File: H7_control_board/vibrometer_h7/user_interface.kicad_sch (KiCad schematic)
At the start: 10 parts, among them SW501 SW_Push, SW502 SW_Push

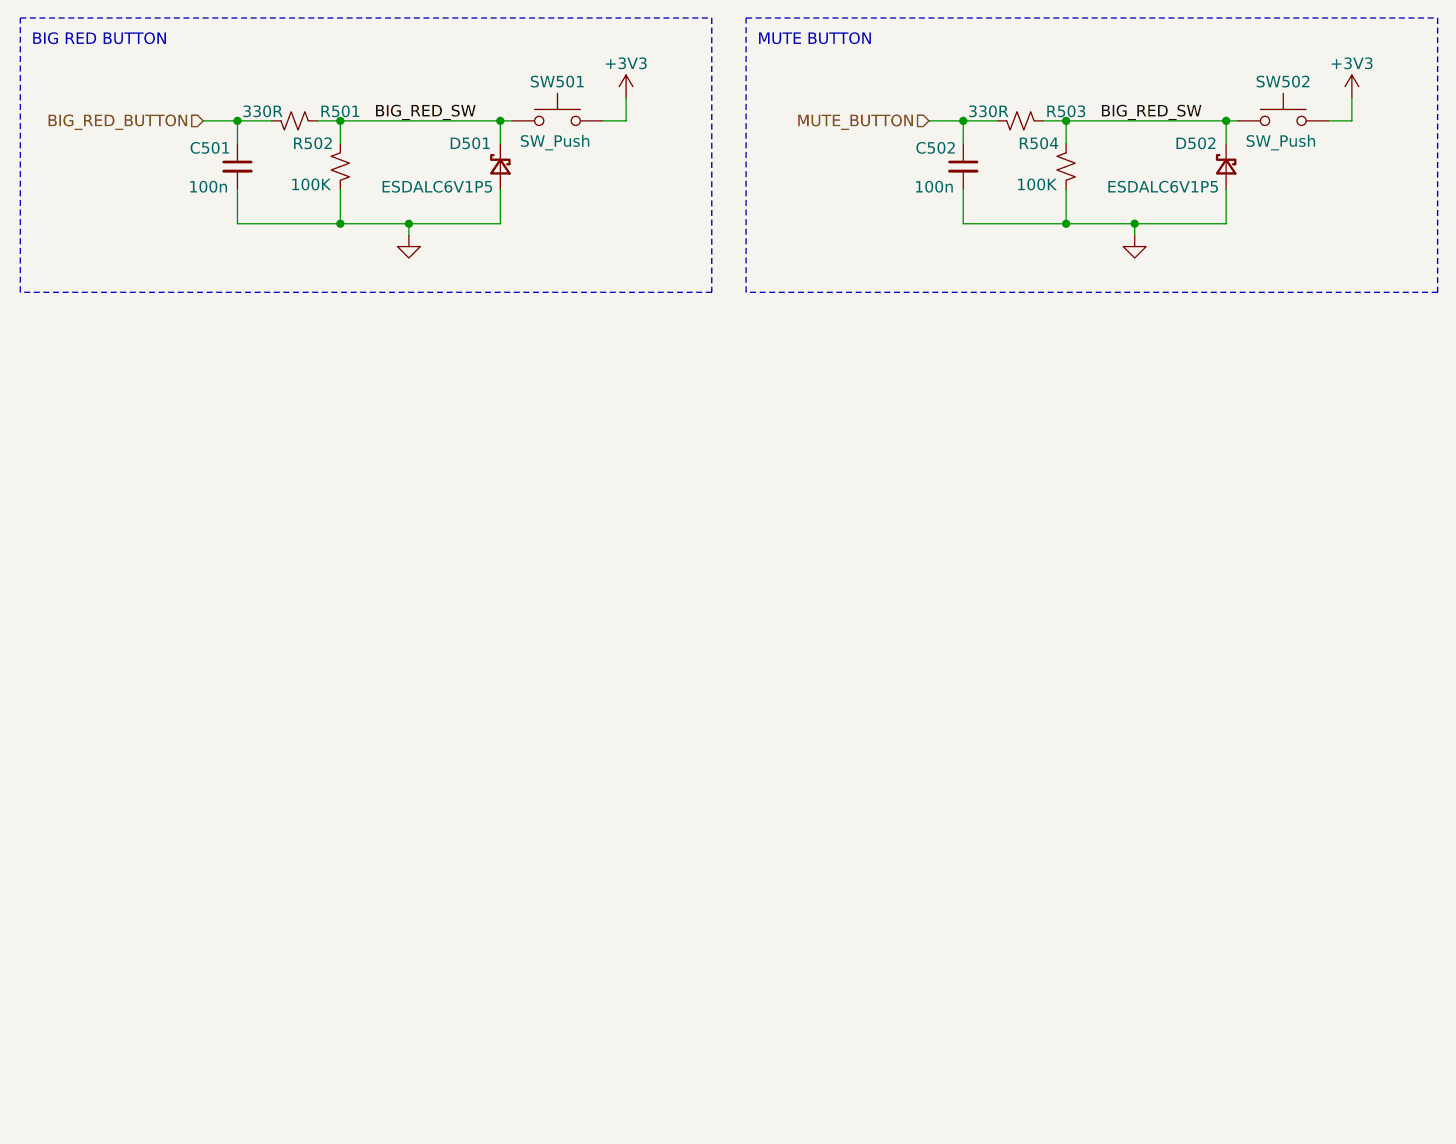
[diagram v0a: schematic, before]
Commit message: more decoupling caps, added level shifter to ws2812 led signal line
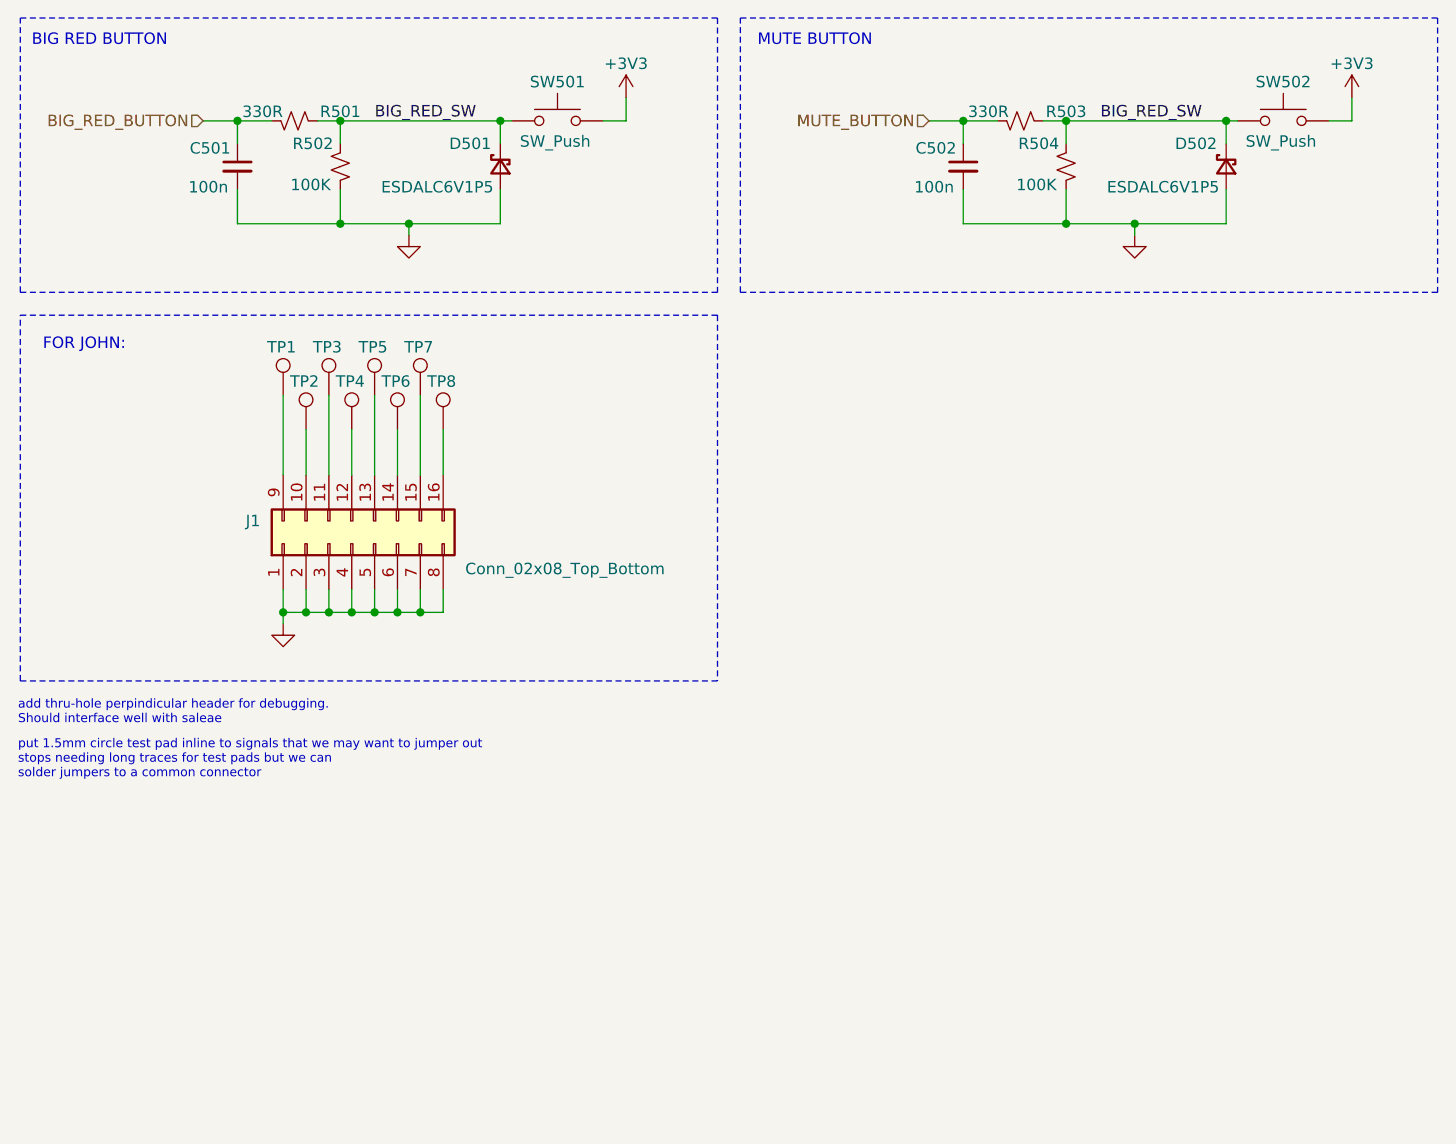
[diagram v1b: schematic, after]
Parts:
- added J1: Conn_02x08_Top_Bottom, symbol Connector_Generic:Conn_02x08_Top_Bottom
- added TP1, TP2, TP3, TP4, TP5, TP6, TP7, TP8: TestPoint, symbol Connector:TestPoint
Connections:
- net GND: now also J1.1 (Pin_1), J1.2 (Pin_2), J1.3 (Pin_3), J1.4 (Pin_4), J1.5 (Pin_5), J1.6 (Pin_6), J1.7 (Pin_7), J1.8 (Pin_8)
- new net: J1.10 (Pin_10), TP2.1
- new net: J1.11 (Pin_11), TP3.1
- new net: J1.12 (Pin_12), TP4.1
- new net: J1.13 (Pin_13), TP5.1
- new net: J1.14 (Pin_14), TP6.1
- new net: J1.15 (Pin_15), TP7.1
- new net: J1.16 (Pin_16), TP8.1
- new net: J1.9 (Pin_9), TP1.1
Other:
- note added: "FOR JOHN:"
- note added: "add thru-hole perpindicular header for debugging. Should interface well with saleae"
- note added: "put 1.5mm circle test pad inline to signals that we may want to jumper out stops needing long traces for test pads but we can solder jumpers to a common connector"

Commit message: selected strobe LEDs, schematic cleanup
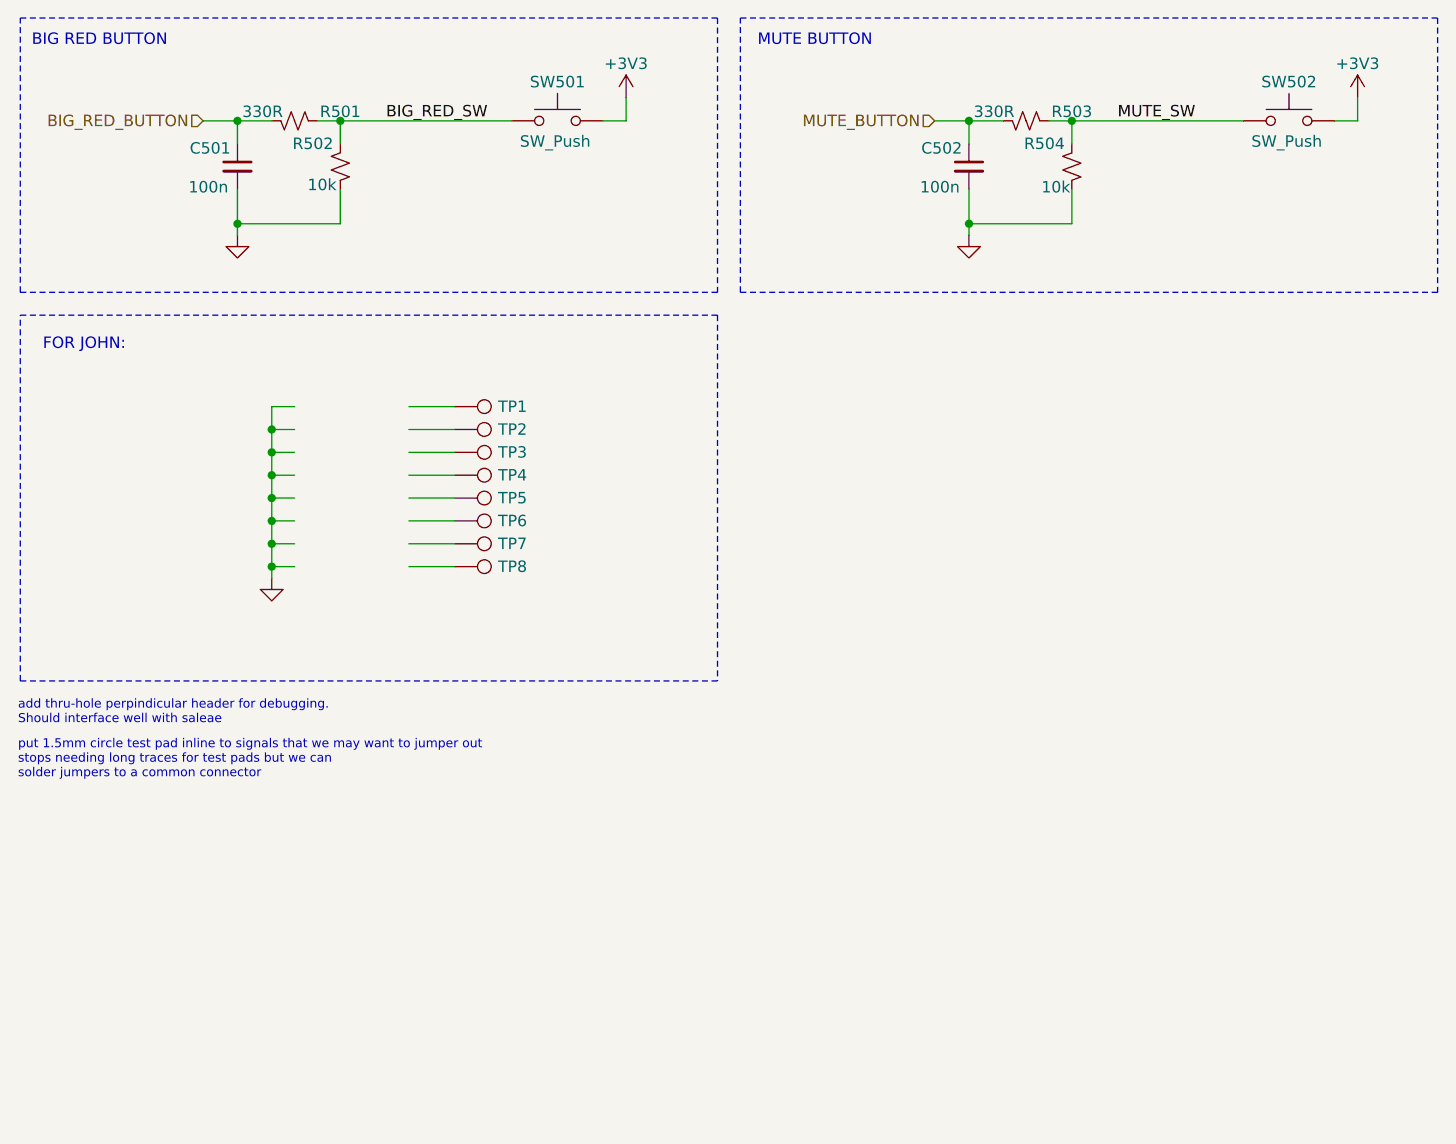
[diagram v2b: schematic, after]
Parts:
- removed D501: ESDALC6V1P5, Package_TO_SOT_SMD:Diodes_SOT-553, symbol Device:D_Schottky_Small
- removed D502: ESDALC6V1P5, symbol Device:D_Schottky_Small
- removed J1: Conn_02x08_Top_Bottom, symbol Connector_Generic:Conn_02x08_Top_Bottom
- R502, R504: value 100K -> 10k
- TP1, TP2, TP3, TP4, TP5, TP6, TP7, TP8: footprint (none) -> TestPoint:TestPoint_Pad_D1.5mm
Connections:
- net BIG_RED_SW: no longer R503.1, R504.2, SW502.2
- new net MUTE_SW: R503.1, R504.2, SW502.2
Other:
- moved on the sheet: C502, R503, R504, SW502, TP1, TP2, TP3, TP4, TP5, TP6, TP7, TP8

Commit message: first pass at board routing
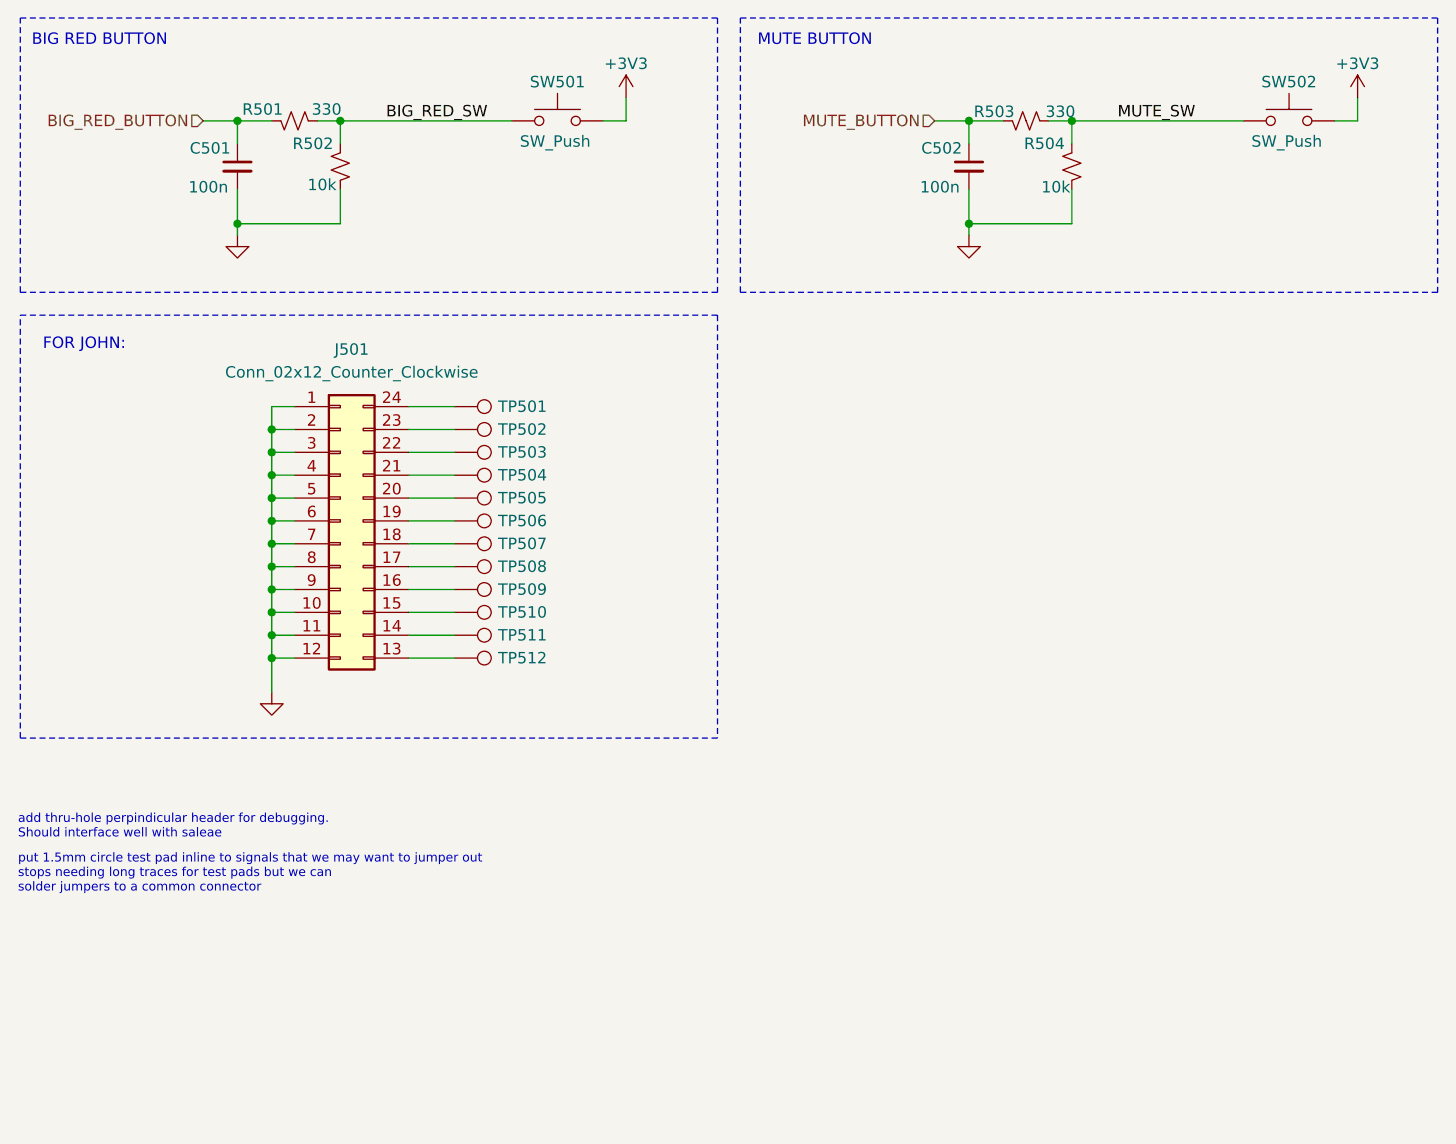
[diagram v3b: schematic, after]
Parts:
- added J501: Conn_02x12_Counter_Clockwise, symbol Connector_Generic:Conn_02x12_Counter_Clockwise
- added TP509, TP510, TP511, TP512: TestPoint, TestPoint:TestPoint_Pad_D1.0mm, symbol Connector:TestPoint
- R501, R503: value 330R -> 330; footprint (none) -> Resistor_SMD:R_0402_1005Metric; LCSC (none) -> C25104
- R502, R504: footprint (none) -> Resistor_SMD:R_0603_1608Metric; LCSC (none) -> C25744
- SW501, SW502: footprint Button_Switch_SMD:SW_Push_1P1T_XKB_TS-1187A -> Button_Switch_SMD:SW_SPST_PTS645; LCSC C318884 -> C3010224
- TP501: renamed from TP1; footprint TestPoint:TestPoint_Pad_D1.5mm -> TestPoint:TestPoint_Pad_D1.0mm
- TP502: renamed from TP2; footprint TestPoint:TestPoint_Pad_D1.5mm -> TestPoint:TestPoint_Pad_D1.0mm
- TP503: renamed from TP3; footprint TestPoint:TestPoint_Pad_D1.5mm -> TestPoint:TestPoint_Pad_D1.0mm
- TP504: renamed from TP4; footprint TestPoint:TestPoint_Pad_D1.5mm -> TestPoint:TestPoint_Pad_D1.0mm
- TP505: renamed from TP5; footprint TestPoint:TestPoint_Pad_D1.5mm -> TestPoint:TestPoint_Pad_D1.0mm
- TP506: renamed from TP6; footprint TestPoint:TestPoint_Pad_D1.5mm -> TestPoint:TestPoint_Pad_D1.0mm
- TP507: renamed from TP7; footprint TestPoint:TestPoint_Pad_D1.5mm -> TestPoint:TestPoint_Pad_D1.0mm
- TP508: renamed from TP8; footprint TestPoint:TestPoint_Pad_D1.5mm -> TestPoint:TestPoint_Pad_D1.0mm
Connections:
- net GND: now also J501.1 (Pin_1), J501.10 (Pin_10), J501.11 (Pin_11), J501.12 (Pin_12), J501.2 (Pin_2), J501.3 (Pin_3), J501.4 (Pin_4), J501.5 (Pin_5), J501.6 (Pin_6), J501.7 (Pin_7), J501.8 (Pin_8), J501.9 (Pin_9)
- net at TP504.1: now also J501.21 (Pin_21)
- net at TP507.1: now also J501.18 (Pin_18)
- net at TP506.1: now also J501.19 (Pin_19)
- net at TP508.1: now also J501.17 (Pin_17)
- net at TP505.1: now also J501.20 (Pin_20)
- net at TP502.1: now also J501.23 (Pin_23)
- net at TP503.1: now also J501.22 (Pin_22)
- net at TP501.1: now also J501.24 (Pin_24)
- new net: J501.13 (Pin_13), TP512.1
- new net: J501.14 (Pin_14), TP511.1
- new net: J501.15 (Pin_15), TP510.1
- new net: J501.16 (Pin_16), TP509.1

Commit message: lots of routing progress!!
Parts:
- removed J501: Conn_02x12_Counter_Clockwise, symbol Connector_Generic:Conn_02x12_Counter_Clockwise
- added J501, J502: Conn_02x08_Odd_Even, Connector_PinHeader_1.00mm:PinHeader_2x08_P1.00mm_Vertical_SMD, symbol Connector_Generic:Conn_02x08_Odd_Even
- added TP513, TP514, TP515, TP516: TestPoint, TestPoint:TestPoint_Pad_D1.0mm, symbol Connector:TestPoint
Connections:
- net GND: now also J501.1 (Pin_1), J501.11 (Pin_11), J501.13 (Pin_13), J501.15 (Pin_15), J501.3 (Pin_3), J501.5 (Pin_5), J501.7 (Pin_7), J501.9 (Pin_9), J502.1 (Pin_1), J502.11 (Pin_11), J502.13 (Pin_13), J502.15 (Pin_15), J502.3 (Pin_3), J502.5 (Pin_5), J502.7 (Pin_7), J502.9 (Pin_9)
- net at TP512.1: now also J502.8 (Pin_8)
- net at TP504.1: now also J501.8 (Pin_8)
- net at TP507.1: now also J501.14 (Pin_14)
- net at TP511.1: now also J502.6 (Pin_6)
- net at TP510.1: now also J502.4 (Pin_4)
- net at TP509.1: now also J502.2 (Pin_2)
- net at TP508.1: now also J501.16 (Pin_16)
- net at TP506.1: now also J501.12 (Pin_12)
- net at TP505.1: now also J501.10 (Pin_10)
- net at TP503.1: now also J501.6 (Pin_6)
- net at TP502.1: now also J501.4 (Pin_4)
- net at TP501.1: now also J501.2 (Pin_2)
- new net: J502.12 (Pin_12), TP514.1
- new net: J502.16 (Pin_16), TP516.1
- new net: J502.14 (Pin_14), TP515.1
- new net: J502.10 (Pin_10), TP513.1
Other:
- moved on the sheet: TP501, TP502, TP503, TP504, TP505, TP506, TP507, TP508
